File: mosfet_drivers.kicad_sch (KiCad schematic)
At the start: 30 parts, among them U6 IR2184, U7 IR2184, U8 IR2184

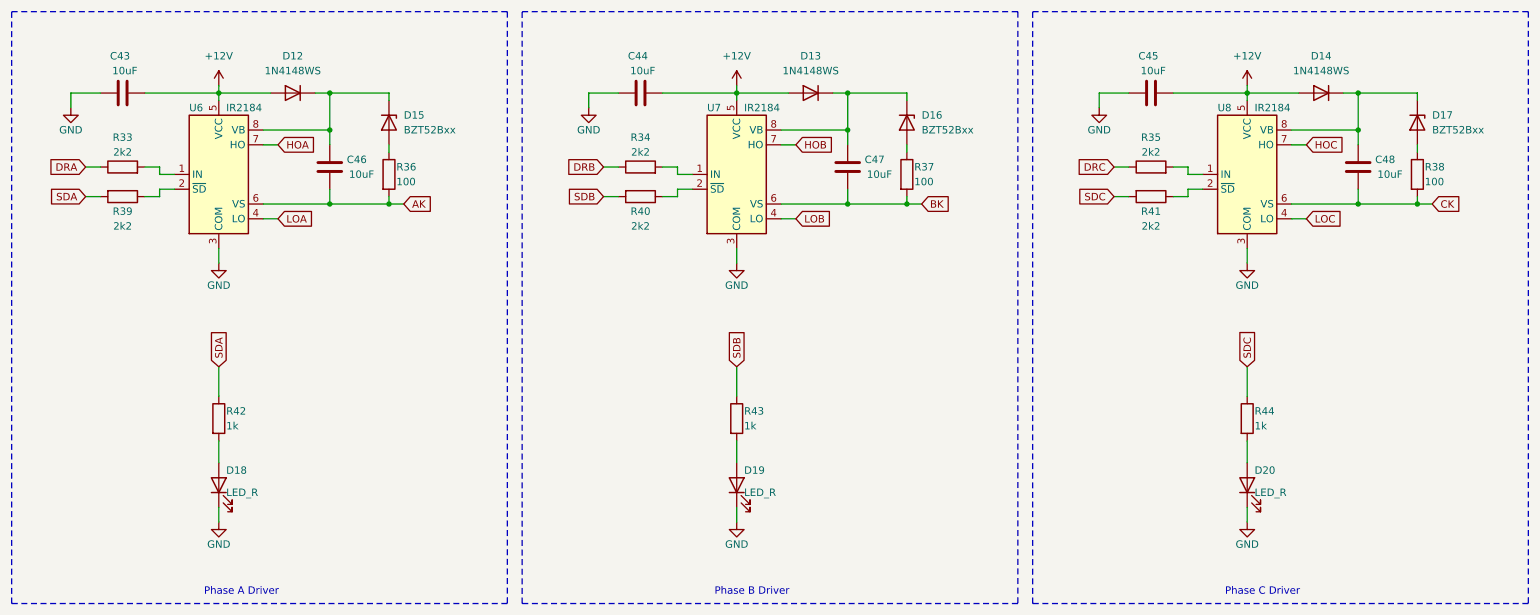
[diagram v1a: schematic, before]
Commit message: Major update on results of testing first order board and on results of crosscheck
* reworked mainswitch scheme
* mainswitch divider. expected commutation time - 2us
* added 3v3bt and 3v3hall
* tvs on hall
* divided 5vhall, 3vhall, 3vbt
* fix misplacement gnd and 3v3 at the BT connector
* fix motorbut (now pullup and gnd on button)
* fix opto gate

+ a lot of minors
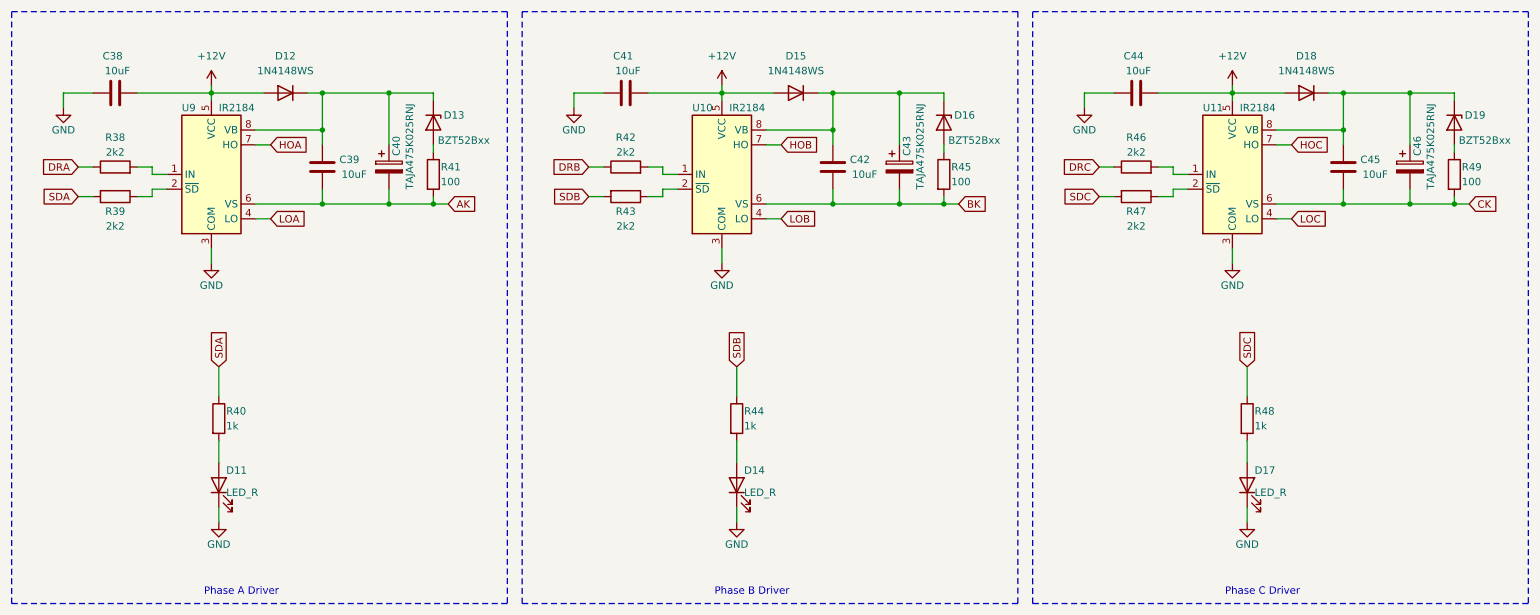
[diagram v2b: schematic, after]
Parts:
- removed C47, C48: 10uF, Capacitor_SMD:C_0603_1608Metric_Pad1.08x0.95mm_HandSolder, symbol Device:C
- removed D13, D14: 1N4148WS, Diode_SMD:D_SOD-323, symbol Diode:1N4148WS
- removed D17: BZT52Bxx, Diode_SMD:D_SOD-123F, symbol Diode:BZT52Bxx
- removed R34, R35, R40, R41: 2k2, Resistor_SMD:R_0603_1608Metric_Pad0.98x0.95mm_HandSolder, symbol Device:R
- removed R37, R38: 100, Resistor_SMD:R_0603_1608Metric_Pad0.98x0.95mm_HandSolder, symbol Device:R
- removed U7, U8: IR2184, Package_SO:SOIC-8-1EP_3.9x4.9mm_P1.27mm_EP2.514x3.2mm_ThermalVias, symbol Driver_FET:IR2184
- added C40, C43, C46: TAJA475K025RNJ, Capacitor_Tantalum_SMD_AKL:CP_EIA-3216-18_Kemet-A, symbol Capacitor_AKL:CP_SMD_Tantalum_Kemet-A_3216
- added C41, C42: 10uF, Capacitor_SMD:C_0603_1608Metric_Pad1.08x0.95mm_HandSolder, symbol Device:C
- added D15, D18: 1N4148WS, Diode_SMD:D_SOD-323, symbol Diode:1N4148WS
- added D19: BZT52Bxx, Diode_SMD:D_SOD-123F, symbol Diode:BZT52Bxx
- added R42, R43, R46, R47: 2k2, Resistor_SMD:R_0603_1608Metric_Pad0.98x0.95mm_HandSolder, symbol Device:R
- added R45, R49: 100, Resistor_SMD:R_0603_1608Metric_Pad0.98x0.95mm_HandSolder, symbol Device:R
- added U10, U11: IR2184, Package_SO:SOIC-8-1EP_3.9x4.9mm_P1.27mm_EP2.514x3.2mm_ThermalVias, symbol Driver_FET:IR2184
- renumbered C43 to C38, C46 to C39, D18 to D11, D15 to D13, D19 to D14, D20 to D17, R33 to R38, R42 to R40, R36 to R41, R43 to R44, R44 to R48, U6 to U9
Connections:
- net +12V: now also C41.2, D15.2 (A), D18.2 (A), U10.5 (VCC), U11.5 (VCC); no longer C45.2
- net AK: now also C40.2
- net BK: now also C42.2, C43.2, R45.2, U10.6 (VS)
- net CK: now also C45.2, C46.2, R49.2, U11.6 (VS)
- net DRB: now also R42.1
- net DRC: now also R46.1
- net GND: now also C41.1, U10.3 (COM), U11.3 (COM); no longer C45.1
- net HOB: now also U10.7 (HO)
- net HOC: now also U11.7 (HO)
- net LOB: now also U10.4 (LO)
- net LOC: now also U11.4 (LO)
- net SDB: now also R43.2
- net SDC: now also R47.2
- net at C39.1, D12.1 (K), D13.1 (K)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: now also C40.1
- net at D16.1 (K): now also C42.1, C43.1, D15.1 (K), U10.8 (VB)
- net at D16.2 (A): now also R45.1
- new net: R47.1, U11.2 (~{SD})
- new net: C45.1, C46.1, D18.1 (K), D19.1 (K), U11.8 (VB)
- new net: R42.2, U10.1 (IN)
- new net: R46.2, U11.1 (IN)
- new net: R43.1, U10.2 (~{SD})
- new net: D19.2 (A), R49.1
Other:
- moved on the sheet: C38, C39, D12, D13, R38, R39, R41, U9
